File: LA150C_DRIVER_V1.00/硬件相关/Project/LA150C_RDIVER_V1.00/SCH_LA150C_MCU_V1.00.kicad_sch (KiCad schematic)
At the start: 14 parts, among them U1 GD32F503REL7, X1 CSTCE8M00G52-R0

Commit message: chore: save LA150C schematic updates
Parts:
- renumbered C34 to C11, C35 to C12, C33 to C13, C32 to C14, C28 to C15, C29 to C16, C30 to C17, C31 to C18, C36 to C19, C37 to C20, C38 to C21, R33 to R9, U1 to U2
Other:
- moved on the sheet: C12, C13, C14, C15, C16, C17, C18, C20, C21, X1

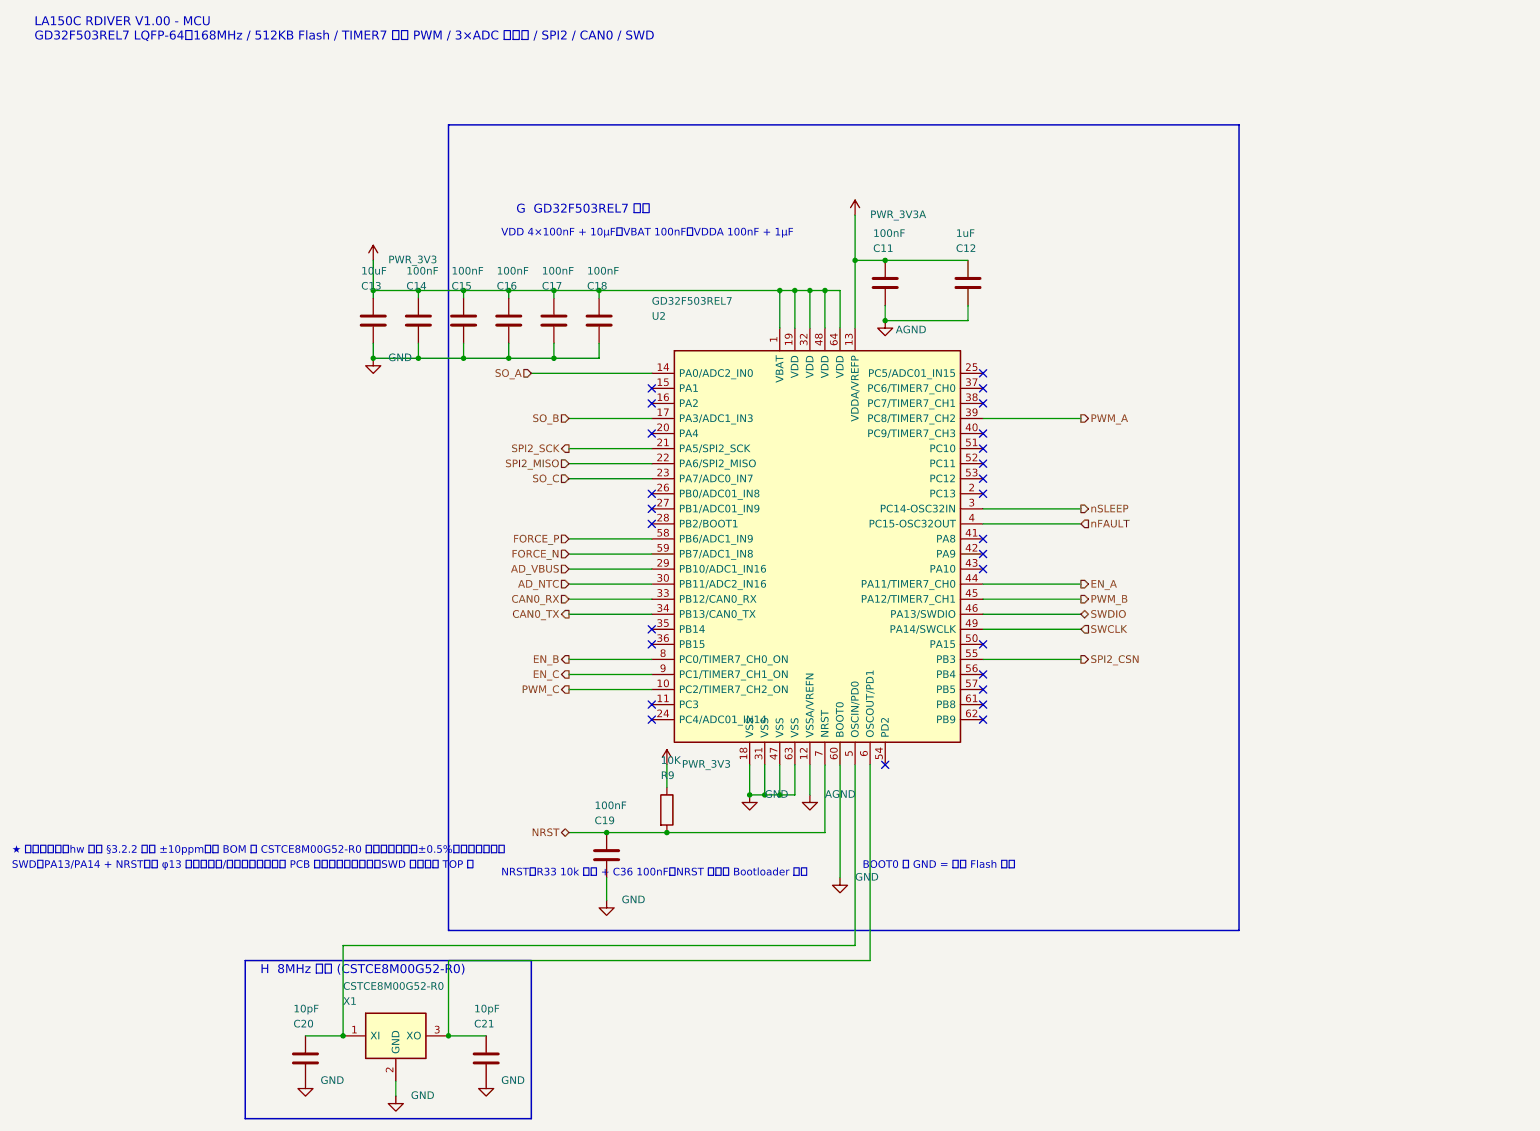
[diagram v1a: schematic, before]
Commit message: feat: finalize LA150C driver schematic
Align the GD32F503 BGA64 pin resources with QS01 V1.12, retain the SCT2230, MT6701 and CAN FD circuits, replace the motor test points with 1.0 x 2.0 mm solder pads, and update the symbols, footprints, ERC report, netlist, BOM and PDF.
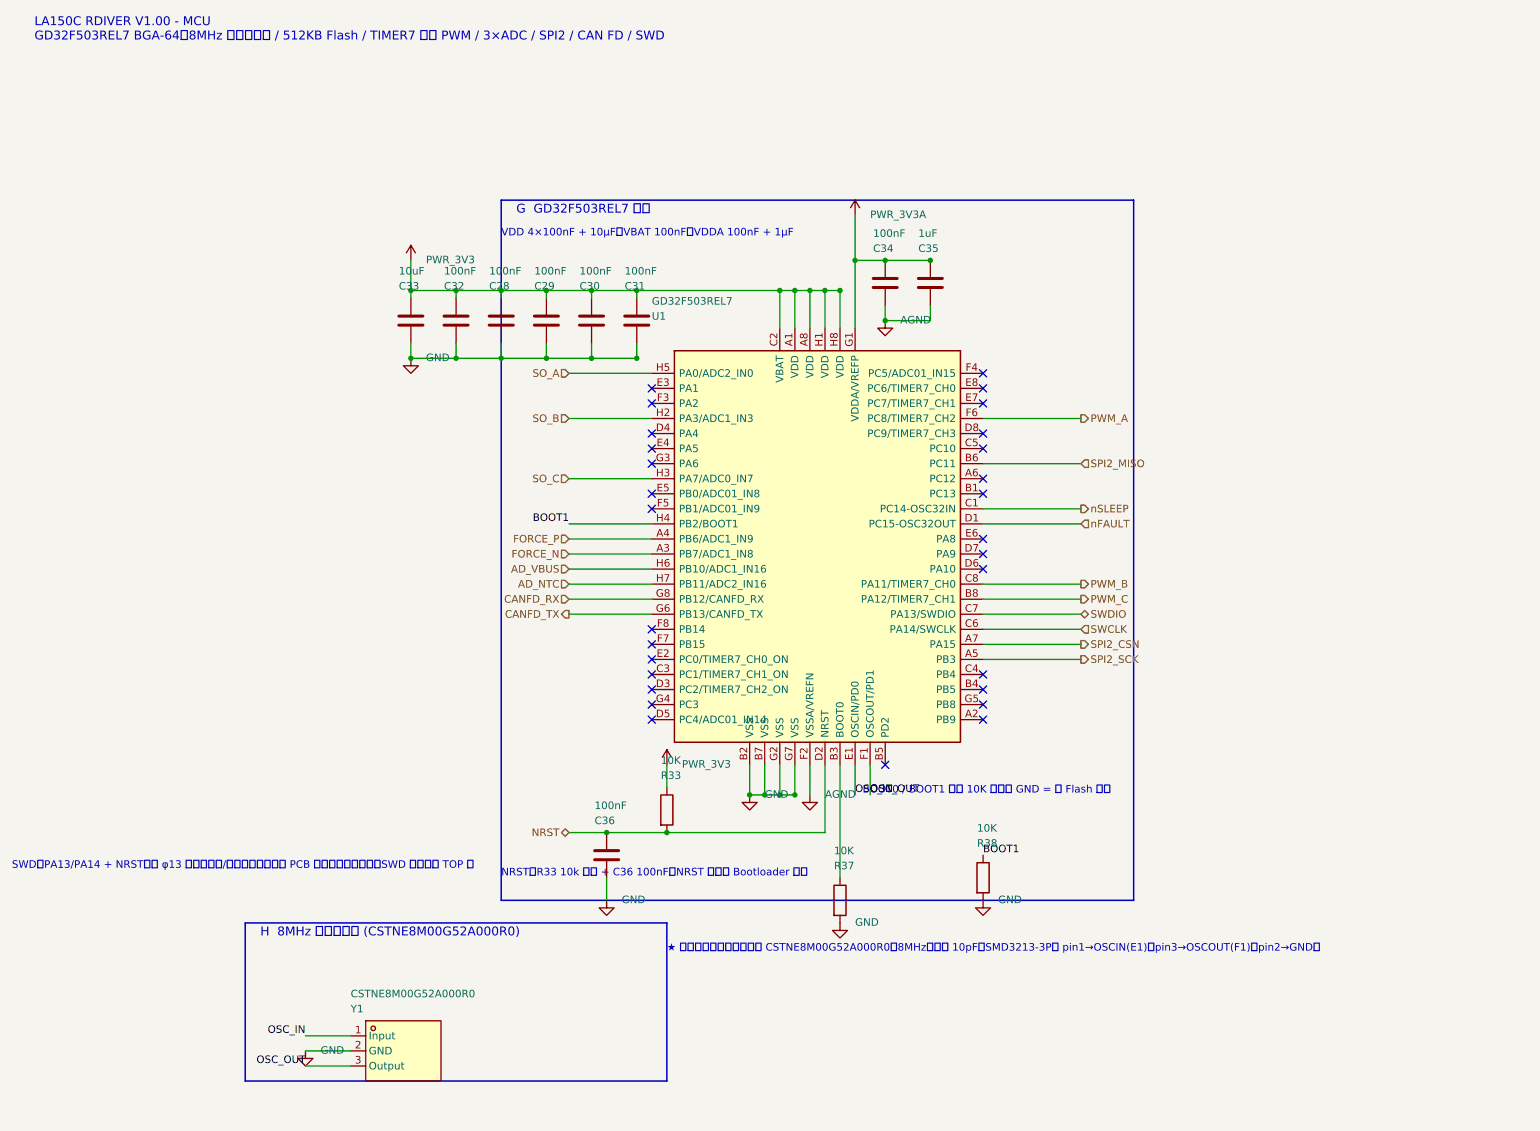
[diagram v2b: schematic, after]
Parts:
- removed C20, C21: 10pF, symbol Device:C
- removed X1: CSTCE8M00G52-R0, symbol LA150C_RDIVER_V1.00:CSTCE8M00G52-R0
- added R37, R38: 10K, Resistors:R0201, symbol LA150C_RDIVER_V1.00:RC0201FR-0710KL
- added Y1: CSTNE8M00G52A000R0, Crystals, Oscillators, Resonators:CRYSTAL-SMD_3P-L3.2-W1.3-P1.2-BL-1, symbol LA150C_RDIVER_V1.00:CSTNE8M00G52A000R0
- C28: renamed from C15; Manufacturer muRata(村田) -> muRata
- C29: renamed from C16; Manufacturer muRata(村田) -> muRata
- C30: renamed from C17; Manufacturer muRata(村田) -> muRata
- C31: renamed from C18; Manufacturer muRata(村田) -> muRata
- C32: renamed from C14; Manufacturer muRata(村田) -> muRata
- C33: renamed from C13; footprint (none) -> Capacitors:C_0603_1608Metric; symbol Device:C -> LA150C_RDIVER_V1.00:GRM188Z71A106KA73D; LCSC Part (none) -> C2959727; MPN (none) -> GRM188Z71A106KA73D; Manufacturer (none) -> muRata(村田)
- C34: renamed from C11; Manufacturer muRata(村田) -> muRata
- C35: renamed from C12; Manufacturer SAMSUNG(三星) -> Samsung Electro-Mechanics
- C36: renamed from C19; Manufacturer muRata(村田) -> muRata
- R33: renamed from R9; Manufacturer YAGEO(国巨) -> YAGEO
- U1: renamed from U2; footprint (none) -> Embedded Processors & Controllers:ucBGA-64_4x4mm_Layout8x8_P0.4mm
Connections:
- net AD_NTC: now also U1.H7 (PB11/ADC2_IN16); no longer U1.30 (PB11/ADC2_IN16)
- net AD_VBUS: now also U1.H6 (PB10/ADC1_IN16); no longer U1.29 (PB10/ADC1_IN16)
- net AGND: now also U1.F2 (VSSA/VREFN); no longer U1.12 (VSSA/VREFN)
- net FORCE_N: now also U1.A3 (PB7/ADC1_IN8); no longer U1.59 (PB7/ADC1_IN8)
- net FORCE_P: now also U1.A4 (PB6/ADC1_IN9); no longer U1.58 (PB6/ADC1_IN9)
- net GND: now also U1.B2 (VSS), U1.B7 (VSS), U1.G2 (VSS), U1.G7 (VSS), R37.2, R38.2, Y1.2 (GND); no longer U1.18 (VSS), U1.31 (VSS), U1.47 (VSS), U1.60 (BOOT0), U1.63 (VSS)
- net NRST: now also U1.D2 (NRST); no longer U1.7 (NRST)
- net PWM_A: now also U1.F6 (PC8/TIMER7_CH2); no longer U1.39 (PC8/TIMER7_CH2)
- net PWM_B: now also U1.C8 (PA11/TIMER7_CH0); no longer U1.45 (PA12/TIMER7_CH1)
- net PWM_C: now also U1.B8 (PA12/TIMER7_CH1); no longer U1.10 (PC2/TIMER7_CH2_ON)
- net PWR_3V3: now also U1.A1 (VDD), U1.A8 (VDD), U1.C2 (VBAT), U1.H1 (VDD), U1.H8 (VDD); no longer U1.1 (VBAT), U1.19 (VDD), U1.32 (VDD), U1.48 (VDD), U1.64 (VDD)
- net PWR_3V3A: now also U1.G1 (VDDA/VREFP); no longer U1.13 (VDDA/VREFP)
- net SO_A: now also U1.H5 (PA0/ADC2_IN0); no longer U1.14 (PA0/ADC2_IN0)
- net SO_B: now also U1.H2 (PA3/ADC1_IN3); no longer U1.17 (PA3/ADC1_IN3)
- net SO_C: now also U1.H3 (PA7/ADC0_IN7); no longer U1.23 (PA7/ADC0_IN7)
- net SPI2_CSN: now also U1.A7 (PA15); no longer U1.55 (PB3)
- net SPI2_MISO: now also U1.B6 (PC11); no longer U1.22 (PA6/SPI2_MISO)
- net SPI2_SCK: now also U1.A5 (PB3); no longer U1.21 (PA5/SPI2_SCK)
- net SWCLK: now also U1.C6 (PA14/SWCLK); no longer U1.49 (PA14/SWCLK)
- net SWDIO: now also U1.C7 (PA13/SWDIO); no longer U1.46 (PA13/SWDIO)
- net nFAULT: now also U1.D1 (PC15-OSC32OUT); no longer U1.4 (PC15-OSC32OUT)
- net nSLEEP: now also U1.C1 (PC14-OSC32IN); no longer U1.3 (PC14-OSC32IN)
- removed net CAN0_RX: U1.33 (PB12/CAN0_RX)
- removed net CAN0_TX: U1.34 (PB13/CAN0_TX)
- removed net EN_A: U1.44 (PA11/TIMER7_CH0)
- removed net EN_B: U1.8 (PC0/TIMER7_CH0_ON)
- removed net EN_C: U1.9 (PC1/TIMER7_CH1_ON)
- new net: R37.1, U1.B3 (BOOT0)
- new net BOOT1: R38.1, U1.H4 (PB2/BOOT1)
- new net CANFD_RX: U1.G8 (PB12/CANFD_RX)
- new net CANFD_TX: U1.G6 (PB13/CANFD_TX)
- new net OSC_IN: U1.E1 (OSCIN/PD0), Y1.1 (Input)
- new net OSC_OUT: U1.F1 (OSCOUT/PD1), Y1.3 (Output)
- no-connect marks 27 -> 29
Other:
- note added: "BOOT0 / BOOT1 均经 10K 下拉到 GND = 主 Flash 启动"
- note added: "H 8MHz 外部谐振器 (CSTNE8M00G52A000R0)"
- note added: "LA150C RDIVER V1.00 - MCU GD32F503REL7 BGA-64：8MHz 外部谐振器 / 512KB Flash / TIMER7 三相 PWM / 3×ADC / SPI2 / CAN FD / SWD"
- note added: "★ 时钟采用外置驱动器同款 CSTNE8M00G52A000R0：8MHz、内置 10pF、SMD3213-3P； pin1→OSCIN(E1)，pin3→OSCOUT(F1)，pin2→GND。"
- note removed: "BOOT0 接 GND = 从主 Flash 启动"
- note removed: "H 8MHz 时钟 (CSTCE8M00G52-R0)"
- note removed: "LA150C RDIVER V1.00 - MCU GD32F503REL7 LQFP-64：168MHz / 512KB Flash / TIMER7 三相 PWM / 3×ADC 注入组 / SPI2 / CAN0 / SWD"
- note removed: "★ 时钟源冲突：hw 设计 §3.2.2 要求 ±10ppm，而 BOM 的 CSTCE8M00G52-R0 是陶瓷谐振器（±0.5%），须重新选型"
- moved on the sheet: C28, C29, C30, C31, C32, C33, C35
